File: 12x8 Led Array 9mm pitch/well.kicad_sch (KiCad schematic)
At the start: 3 parts

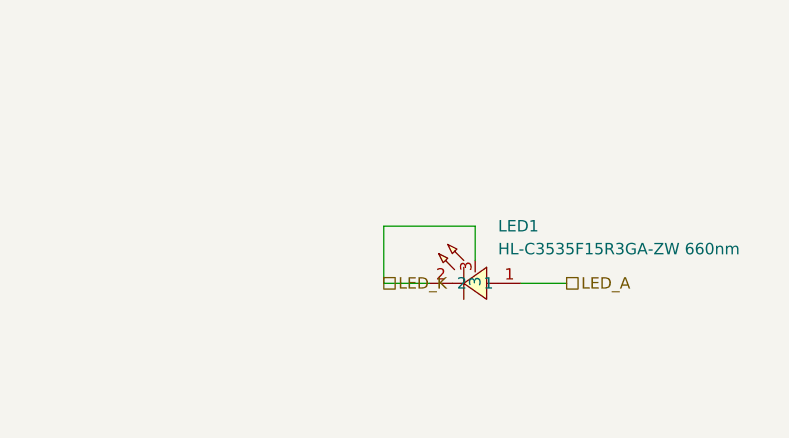
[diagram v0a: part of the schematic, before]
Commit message: Apply user's label cleanup style to control board
- All generated labels now carry explicit justification (left/right
  per rotation, bottom-anchored) matching the hand-cleaned LED board
- gen_schematics_hier.py takes led|ctl|all arg; LED board excluded
  from regeneration by default (hand-edited in KiCad)
- Control board netlist re-verified: all 412 nets match

Co-Authored-By: Claude Fable 5 <noreply@anthropic.com>
Claude-Session: https://claude.ai/code/session_017oD54uh7Tvu54u9NPQNcZB
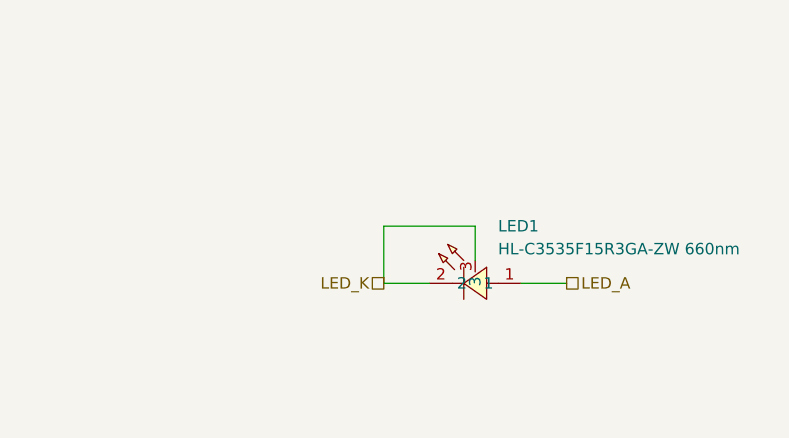
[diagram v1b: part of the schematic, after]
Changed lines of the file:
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@@
 	(hierarchical_label "LED_K"
 		(shape passive)
-		(at 66.04 64.77 0)
+		(at 66.04 64.77 180)
 		(effects
 			(font
 				(size 1.27 1.27)
 			)
+			(justify right)
 		)
 	)
@@
 				(size 1.27 1.27)
 			)
+			(justify left)
 		)
 	)
@@
 		)
 	)
-	(sheet_instances
-		(path "/"
-			(page "1")
-		)
-	)

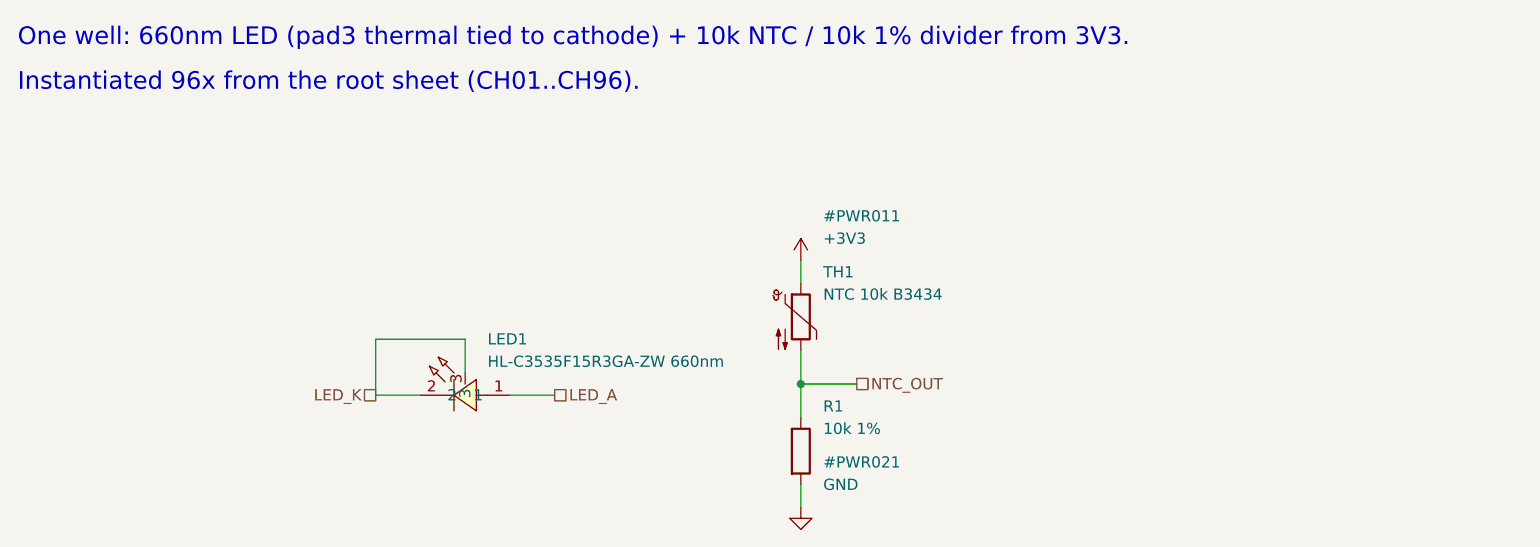
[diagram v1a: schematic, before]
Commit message: Fix 3.3V/GND bridge, adopt +3.3V naming, power symbols at rail pins
- Removed 6 wire segments that tied each mux VCC run into its
  decoupling cap's GND pin (merged the rails through all six caps)
- Renamed +3V3 -> +3.3V everywhere (user convention), incl. well
  sub-sheet power symbols and docs
- Control board root now uses real power symbols on wire stubs
  instead of text labels for GND/+3.3V/+5V/+24V (user style)
- Verified: netlists match design intent on all 300+412 nets; LED
  board ERC 0 violations; I2C addresses confirmed from netlist
  (PCA9685 0x40-0x45, ADS1115 0x48, no conflicts)

Co-Authored-By: Claude Fable 5 <noreply@anthropic.com>
Claude-Session: https://claude.ai/code/session_017oD54uh7Tvu54u9NPQNcZB
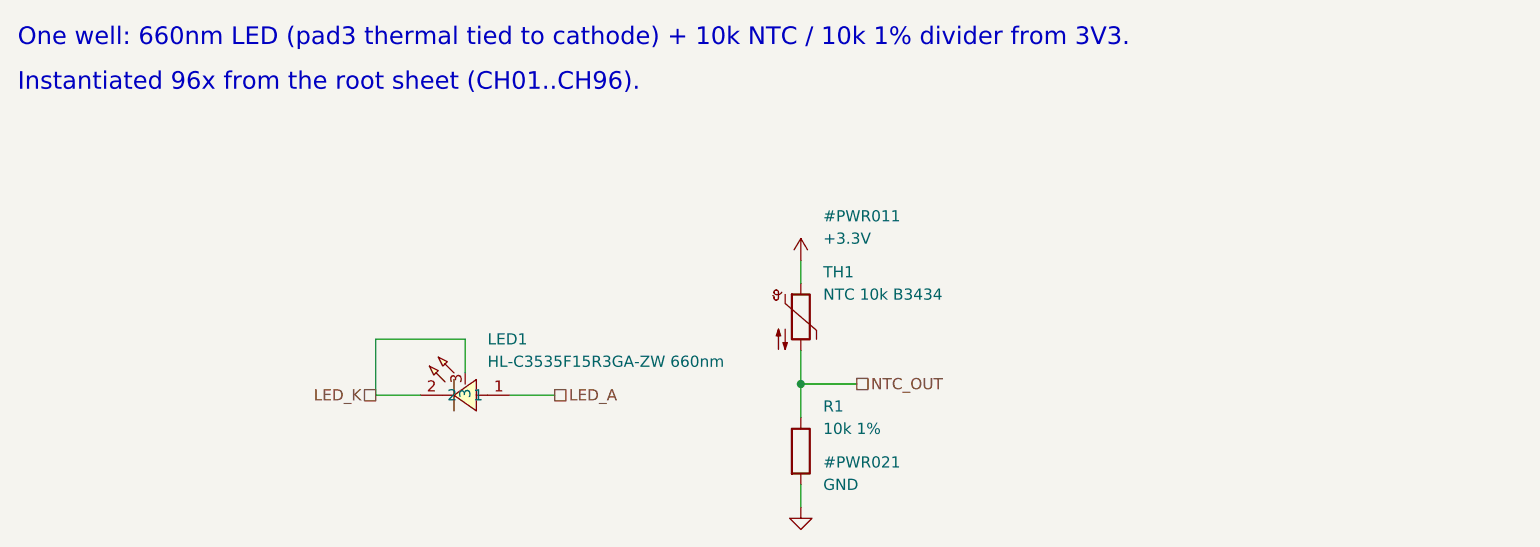
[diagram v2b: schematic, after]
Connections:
- net +3V3 renamed +3.3V
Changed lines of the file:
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@@
 	)
 	(symbol
-		(lib_id "power:+3V3")
+		(lib_id "power:+3.3V")
 		(at 114.3 49.53 0)
 		(unit 1)
@@
 			)
 		)
-		(property "Value" "+3V3"
+		(property "Value" "+3.3V"
 			(at 116.84 46.99 0)
 			(show_name no)

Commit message: Swap to 6x 40-pin IDC ribbons (IDE-safe pinout), clear routing for rearrange
- J1-J6 both boards: 16 channels each = one PCA9685 bank per cable;
  pairs on pins 1-18/21-34, pin 20 NC (IDE key), GND 19+35-40
- Logic ribbon renamed J9; control screw terminal now J12
- Schematics regenerated (netlists verified 300+412), CONNECTIONS
  updated; connectors placed at nominal spots for user rearrangement
- All routing cleared except LED thermal via farms per user request
- New vault note: What Every Part Does

Co-Authored-By: Claude Fable 5 <noreply@anthropic.com>
Claude-Session: https://claude.ai/code/session_017oD54uh7Tvu54u9NPQNcZB
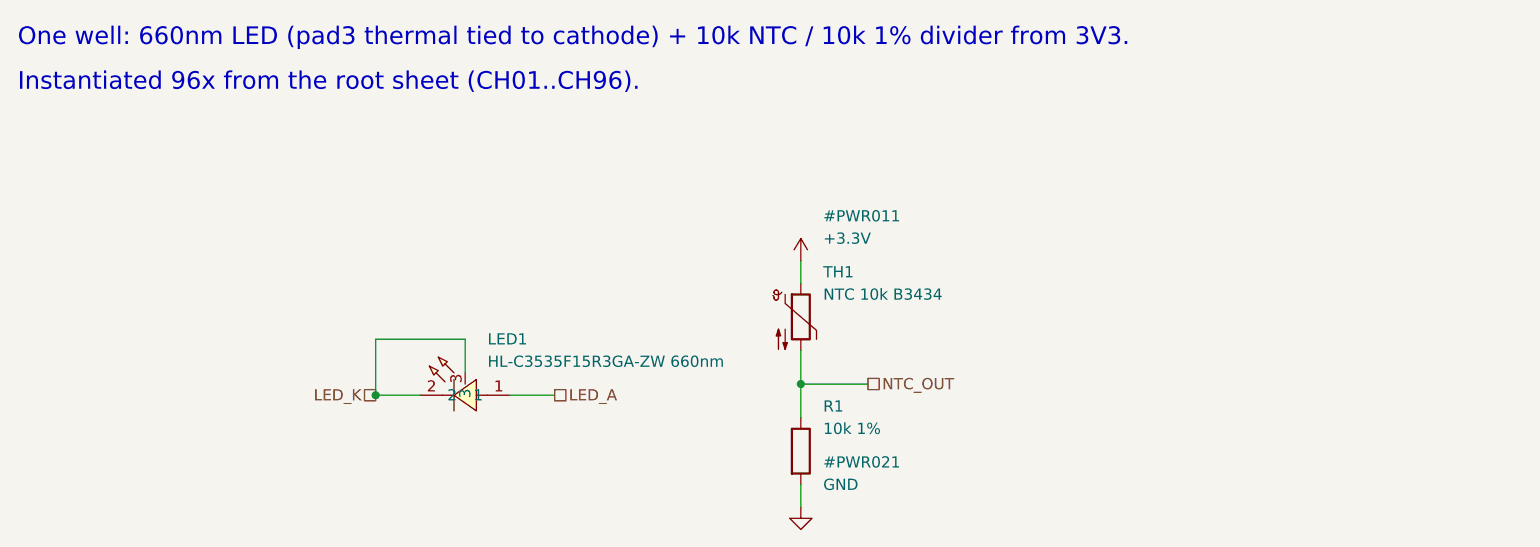
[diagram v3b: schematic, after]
